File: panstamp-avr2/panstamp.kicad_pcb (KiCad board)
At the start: 4 copper layers, 16 x 22 mm, 30 parts, among them P1 CONN_01X10, P2 CONN_01X10, P3 CONN_01X07, P4 CONN_01X07, U1 ATMEGA328P, U2 CC1101, U3 BALUN+FILTER, X1 26MHz

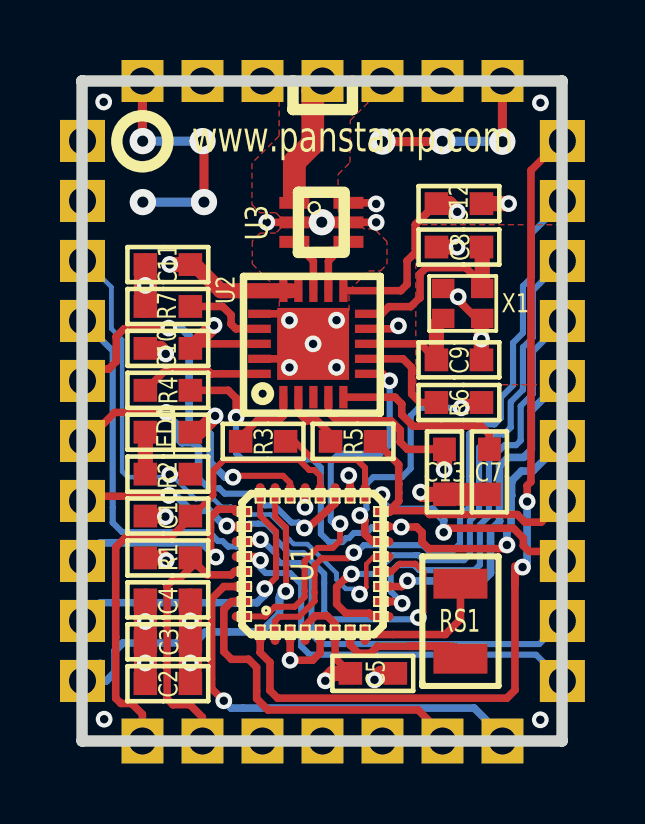
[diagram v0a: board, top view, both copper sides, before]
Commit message: Fiducials added to the PCB
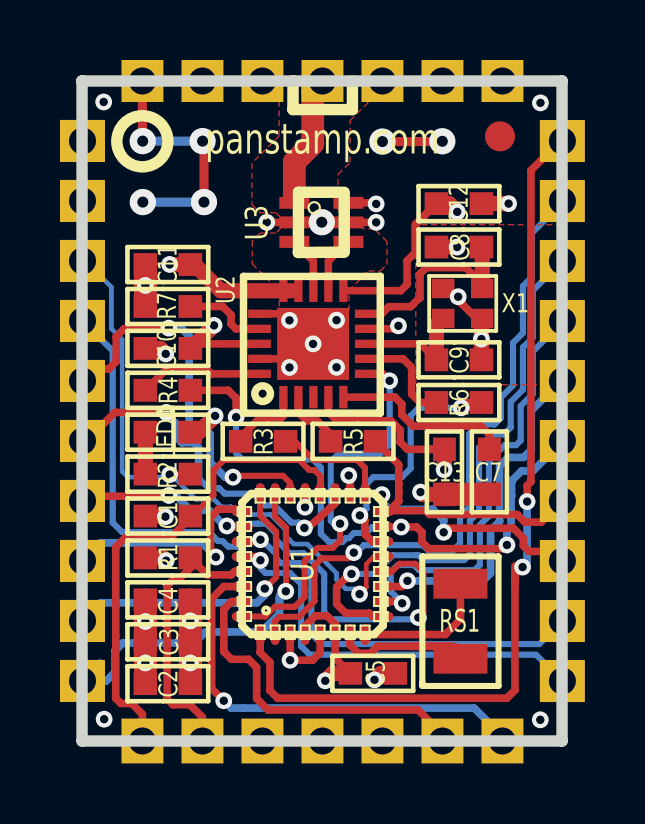
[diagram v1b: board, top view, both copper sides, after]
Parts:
- added fiducial: VAL**, mymods:fiducial, F.Cu at (162.1, 114.8)
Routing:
- net GND: track 79.6 -> 73.6 mm, vias 34 -> 33
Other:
- board text added: "panstamp.com"
- board text removed: "www.panstamp.com"
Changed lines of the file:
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@@
-(kicad_pcb (version 4) (host pcbnew "(2014-jul-16 BZR unknown)-product")
+(kicad_pcb (version 4) (host pcbnew no-vcs-found-product)
   (general
     (links 95)
     (no_connects 0)
-    (area 147.927699 112.714699 164.308701 135.095701)
+    (area 137.9874 109.0042 174.013601 140.7914)
     (thickness 1.6002)
     (drawings 15)
-    (tracks 834)
+    (tracks 828)
     (zones 0)
-    (modules 30)
+    (modules 31)
     (nets 45)
   )
@@
   )
   (setup
-    (last_trace_width 0.508)
+    (last_trace_width 0.1524)
     (user_trace_width 0.2032)
     (user_trace_width 0.254)
@@
       (xy 13.208 -5.2324)) (layer B.SilkS) (width 0.00254))
   )
+  (module mymods:fiducial (layer Front)
+    (at 162.05 114.75)
+    (fp_text reference fiducial (at 0.175 -6.175) (layer F.SilkS) hide
+      (effects (font (thickness 0.3048)))
+    )
+    (fp_text value VAL** (at 0.5 -3.95) (layer F.SilkS) hide
+      (effects (font (thickness 0.3048)))
+    )
+    (pad 1 smd circle (at 0 0) (size 1 1) (layers Front F.Mask)
+      (solder_mask_margin 0.5) (clearance 0.5))
+  )
   (gr_line (start 157.13456 113.84788) (end 157.13456 112.90808) (angle 90) (layer B.SilkS) (width 0.381))
   (gr_line (start 155.1432 113.84788) (end 157.13456 113.84788) (angle 90) (layer B.SilkS) (width 0.381))
@@
     (effects (font (size 1.524 1.27) (thickness 0.1778) italic) (justify mirror))
   )
-  (gr_text www.panstamp.com (at 157.1282 114.7852) (layer F.SilkS)
+  (gr_text panstamp.com (at 156.125 114.85) (layer F.SilkS)
     (effects (font (size 1.016 0.762) (thickness 0.1524)))
   )
@@
   (segment (start 162.70224 113.63452) (end 163.3982 113.63452) (width 0.254) (layer Ground) (net 1))
   (segment (start 160.1978 126.6825) (end 161.6964 126.6825) (width 0.762) (layer Front) (net 1))
-  (segment (start 162.1282 114.92992) (end 162.1282 112.9066) (width 0.508) (layer Ground) (net 1))
   (segment (start 162.1282 112.9066) (end 162.1296 112.9052) (width 0.508) (layer Ground) (net 1))
   (segment (start 160.12668 114.91468) (end 160.12668 112.90812) (width 0.508) (layer Ground) (net 1))
@@
   (via (at 150.1394 114.9096) (size 0.8763) (drill 0.3683) (layers Front Back) (net 1))
   (segment (start 150.1296 114.8998) (end 150.1394 114.9096) (width 0.3048) (layer Front) (net 1))
-  (segment (start 162.1296 112.9052) (end 162.1296 114.92852) (width 0.3048) (layer Front) (net 1))
   (segment (start 158.13024 114.92484) (end 158.1404 114.92484) (width 0.3048) (layer Back) (net 1))
   (via (at 158.13024 114.92484) (size 0.8763) (drill 0.3683) (layers Front Back) (net 1))
@@
   (segment (start 160.12668 114.91468) (end 160.11652 114.92484) (width 0.3048) (layer Front) (net 1))
   (via (at 160.12668 114.91468) (size 0.8763) (drill 0.3683) (layers Front Back) (net 1))
-  (segment (start 162.11296 114.91468) (end 160.12668 114.91468) (width 0.3048) (layer Back) (net 1))
-  (segment (start 162.1282 114.92992) (end 162.11296 114.91468) (width 0.3048) (layer Back) (net 1))
-  (via (at 162.1282 114.92992) (size 0.8763) (drill 0.3683) (layers Front Back) (net 1))
-  (segment (start 162.1296 114.92852) (end 162.1282 114.92992) (width 0.3048) (layer Front) (net 1))
   (segment (start 155.194 117.61724) (end 156.9974 117.61724) (width 0.3048) (layer Front) (net 1))
   (segment (start 155.194 117.61724) (end 156.10332 117.61724) (width 0.254) (layer Front) (net 1))
